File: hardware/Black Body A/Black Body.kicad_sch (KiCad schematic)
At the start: 38 parts, among them IC2 MCP96L00T-E_MX, J1 53307-2471, J2 Conn_01x02, J3 Conn_01x04, J5 Conn_02x04_Top_Bottom, J7 Conn_02x03_Top_Bottom

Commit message: new layout 2.0
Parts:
- removed R11, R12: 1.5k, Resistor_SMD:R_0805_2012Metric, symbol Device:R_US
- J3: footprint Connector_Molex:Molex_Nano-Fit_105313-xx04_1x04_P2.50mm_Horizontal -> Connector_PinHeader_2.54mm:PinHeader_1x04_P2.54mm_Vertical
- renumbered Ra1 to R11, Rb1 to R12

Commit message: Updated layout and 3D models
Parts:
- C2: P/N (none) -> MLASU168SB5105KTNA01
- C3: P/N (none) -> MLASH168SB7104KTNA01
- DB_1, DB_2, DB_3, Heartbeat1: P/N (none) -> LS Q976.01-N1Q2-1
- F2: P/N (none) -> 3557-2
- FB1, FB2: P/N (none) -> 742792910
- GND1, TP_TC_1, TP_TC_2, TP_TC_F_1, TP_TC_F_2, VCC1: P/N (none) -> 5015
- I2C_SCL1, I2C_SDA1, INT1: P/N (none) -> TSW-101-07-G-S
- IC2: footprint Blackbody Footprint:QFN65P500X500X100-21N-D -> BlackBody:QFN65P500X500X100-21N-D; P/N (none) -> MCP96L00T-E/MX
- J2: footprint Connector_Molex:Molex_Nano-Fit_105313-xx02_1x02_P2.50mm_Horizontal -> utsvt_connectors:105313-2102
- J7: footprint Connector_Molex:Molex_Nano-Fit_105314-xx06_2x03_P2.50mm_Horizontal -> utsvt_connectors:105314-1306
- R1: P/N (none) -> CRCW080510K0FKEA
- R10, R4, R7, R8: P/N (none) -> CRCW08051K50FKEA
- R11: P/N (none) -> CRCW060310K0FKEI
- R12: P/N (none) -> CRCW060343K0FKEI
- R2, R3: P/N (none) -> CRCW06031K00FKEI
- R5, R6: P/N (none) -> CRCW0603100RFKEA
- R9: P/N (none) -> CRCW06030000Z0EE

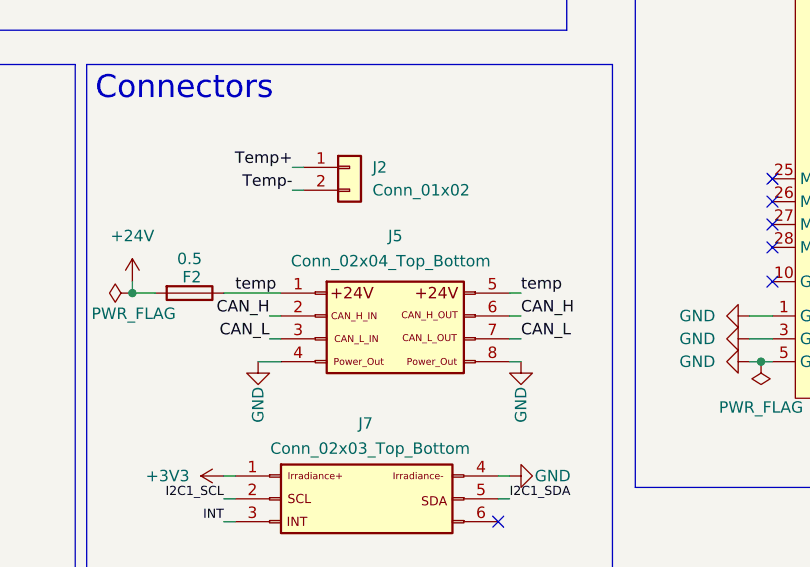
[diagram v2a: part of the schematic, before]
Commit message: changed 3D models for breakout
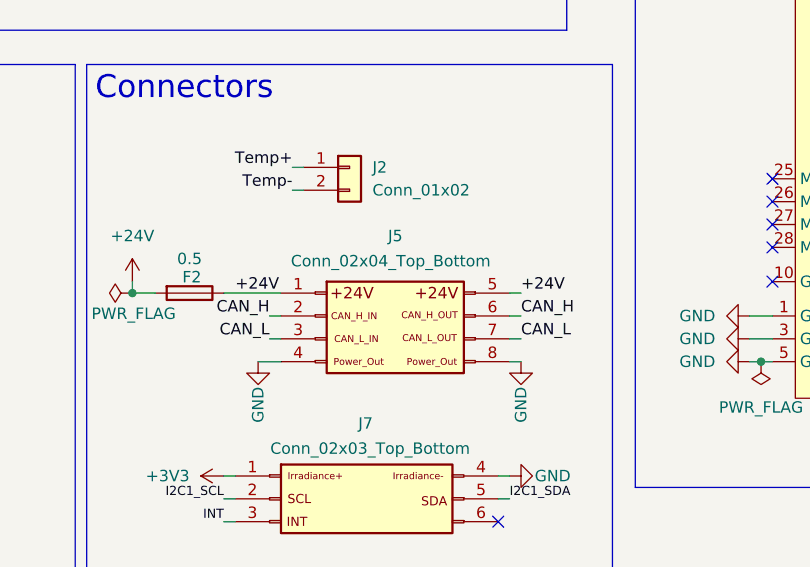
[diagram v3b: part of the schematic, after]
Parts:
- GND1, TP_TC_1, TP_TC_2, TP_TC_F_1, TP_TC_F_2, VCC1: footprint TestPoint:TestPoint_Pad_1.0x1.0mm -> TestPoint:TestPoint_Keystone_5005-5009_Compact
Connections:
- net temp is gone; now on net +24V: F2.1, J5.1 (Pin_1), J5.5 (Pin_5)
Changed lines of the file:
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@@
 		)
 	)
-	(label "temp"
+	(label "+24V"
 		(at 153.67 134.62 0)
 		(effects
@@
 		)
 	)
-	(label "temp"
+	(label "+24V"
 		(at 121.92 134.62 0)
 		(effects
@@
 			)
 		)
-		(property "Footprint" "TestPoint:TestPoint_Pad_1.0x1.0mm"
+		(property "Footprint" "TestPoint:TestPoint_Keystone_5005-5009_Compact"
 			(at 115.57 68.58 0)
 			(effects
@@
 			)
 		)
-		(property "Footprint" "TestPoint:TestPoint_Pad_1.0x1.0mm"
+		(property "Footprint" "TestPoint:TestPoint_Keystone_5005-5009_Compact"
 			(at 88.9 60.96 0)
 			(effects
@@
 			)
 		)
-		(property "Footprint" "TestPoint:TestPoint_Pad_1.0x1.0mm"
+		(property "Footprint" "TestPoint:TestPoint_Keystone_5005-5009_Compact"
 			(at 78.74 68.58 0)
 			(effects
@@
 			)
 		)
-		(property "Footprint" "TestPoint:TestPoint_Pad_1.0x1.0mm"
+		(property "Footprint" "TestPoint:TestPoint_Keystone_5005-5009_Compact"
 			(at 125.73 60.96 0)
 			(effects
@@
 			)
 		)
-		(property "Footprint" "TestPoint:TestPoint_Pad_1.0x1.0mm"
+		(property "Footprint" "TestPoint:TestPoint_Keystone_5005-5009_Compact"
 			(at 224.79 88.9 0)
 			(effects
@@
 			)
 		)
-		(property "Footprint" "TestPoint:TestPoint_Pad_1.0x1.0mm"
+		(property "Footprint" "TestPoint:TestPoint_Keystone_5005-5009_Compact"
 			(at 27.94 165.1 0)
 			(effects

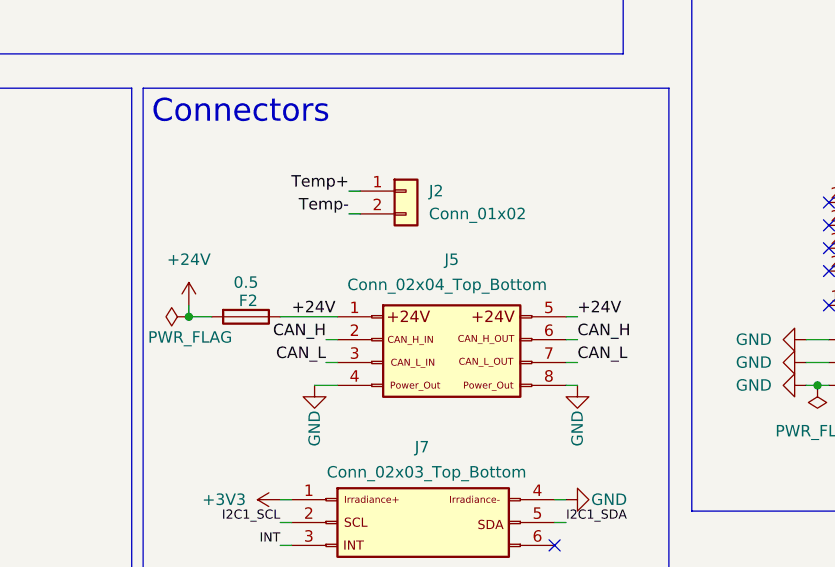
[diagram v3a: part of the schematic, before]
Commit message: updated 24V
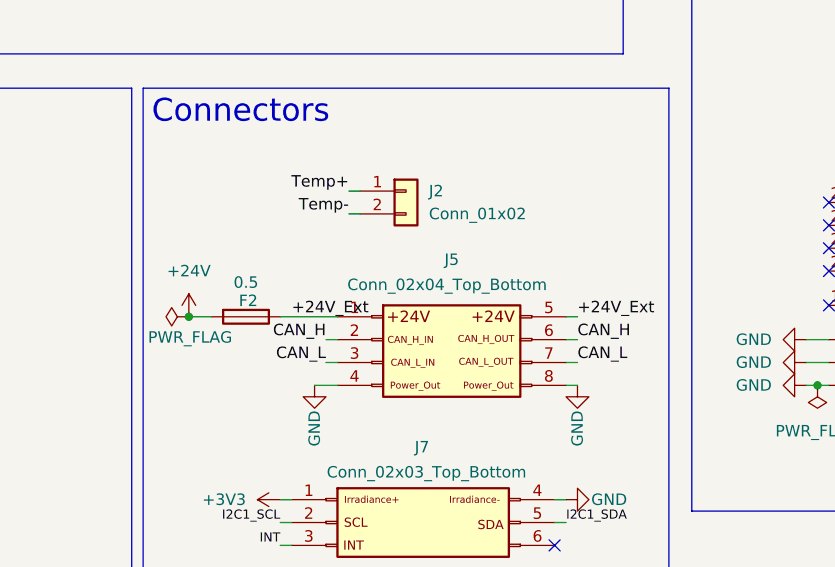
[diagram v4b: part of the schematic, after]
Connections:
- net +24V: no longer F2.1, J5.1 (Pin_1), J5.5 (Pin_5)
- new net +24V_Ext: F2.1, J5.1 (Pin_1), J5.5 (Pin_5)
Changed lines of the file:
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@@
 	)
 	(junction
-		(at 110.49 134.62)
-		(diameter 0)
-		(color 0 0 0 0)
-	)
-	(junction
 		(at 180.34 142.24)
 		(diameter 0)
@@
 	)
 	(junction
+		(at 110.49 134.62)
+		(diameter 0)
+		(color 0 0 0 0)
+	)
+	(junction
 		(at 120.65 60.96)
 		(diameter 0)
@@
 	(wire
 		(pts
-			(xy 110.49 133.35) (xy 110.49 134.62)
-		)
-		(stroke
-			(width 0)
-			(type default)
-		)
-	)
-	(wire
-		(pts
 			(xy 220.98 101.6) (xy 236.22 101.6)
 		)
@@
 		)
 	)
-	(label "+24V"
-		(at 153.67 134.62 0)
-		(effects
-			(font
-				(size 1.27 1.27)
-			)
-			(justify left bottom)
-		)
-	)
 	(label "INT"
 		(at 24.13 130.81 270)
@@
 		)
 	)
+	(label "+24V_Ext"
+		(at 153.67 134.62 0)
+		(effects
+			(font
+				(size 1.27 1.27)
+			)
+			(justify left bottom)
+		)
+	)
 	(label "DB_Conn_2"
 		(at 217.17 139.7 0)
@@
 		)
 	)
-	(label "+24V"
+	(label "+24V_Ext"
 		(at 121.92 134.62 0)
 		(effects
@@
 	)
 	(symbol
-		(lib_id "Connector:TestPoint")
-		(at 83.82 68.58 180)
+		(lib_id "power:+24V")
+		(at 110.49 134.62 0)
 		(unit 1)
 		(exclude_from_sim no)
@@
 		(dnp no)
 		(fields_autoplaced yes)
-		(property "Reference" "TP_TC_F_2"
-			(at 86.36 70.6119 0)
-			(effects
-				(font
-					(size 1.27 1.27)
-				)
-				(justify right)
-			)
-		)
-		(property "Value" "TestPoint"
-			(at 86.36 73.1519 0)
-			(effects
-				(font
-					(size 1.27 1.27)
-				)
-				(justify right)
-			)
-		)
-		(property "Footprint" "TestPoint:TestPoint_Keystone_5005-5009_Compact"
-			(at 78.74 68.58 0)
+		(property "Reference" "#PWR09"
+			(at 110.49 138.43 0)
 			(effects
 				(font
@@
 			)
 		)
-		(property "Datasheet" "~"
-			(at 78.74 68.58 0)
+		(property "Value" "+24V"
+			(at 110.49 129.54 0)
 			(effects
 				(font
 					(size 1.27 1.27)
 				)
-				(hide yes)
 			)
 		)
-		(property "Description" "test point"
-			(at 83.82 68.58 0)
+		(property "Footprint" ""
+			(at 110.49 134.62 0)
 			(effects
 				(font
@@
 			)
 		)
-		(property "Sim.Device" ""
-			(at 83.82 68.58 0)
+		(property "Datasheet" ""
+			(at 110.49 134.62 0)
 			(effects
 				(font
@@
 			)
 		)
-		(property "P/N" "5015 "
-			(at 83.82 68.58 0)
+		(property "Description" "Power symbol creates a global label with name \"+24V\""
+			(at 110.49 134.62 0)
 			(effects
 				(font
@@
 			(project "Black Body"
 				(path "/326551d7-59c6-4bc5-b0df-e38f608d8925"
-					(reference "TP_TC_F_2")
+					(reference "#PWR09")
 					(unit 1)
 				)
@@
 	)
 	(symbol
-		(lib_id "power:+24V")
-		(at 110.49 133.35 0)
+		(lib_id "Connector:TestPoint")
+		(at 83.82 68.58 180)
 		(unit 1)
 		(exclude_from_sim no)
@@
 		(dnp no)
 		(fields_autoplaced yes)
-		(property "Reference" "#PWR013"
-			(at 110.49 137.16 0)
+		(property "Reference" "TP_TC_F_2"
+			(at 86.36 70.6119 0)
+			(effects
+				(font
+					(size 1.27 1.27)
+				)
+				(justify right)
+			)
+		)
+		(property "Value" "TestPoint"
+			(at 86.36 73.1519 0)
+			(effects
+				(font
+					(size 1.27 1.27)
+				)
+				(justify right)
+			)
+		)
+		(property "Footprint" "TestPoint:TestPoint_Keystone_5005-5009_Compact"
+			(at 78.74 68.58 0)
 			(effects
 				(font
@@
 			)
 		)
-		(property "Value" "+24V"
-			(at 110.49 128.27 0)
+		(property "Datasheet" "~"
+			(at 78.74 68.58 0)
 			(effects
 				(font
 					(size 1.27 1.27)
 				)
+				(hide yes)
 			)
 		)
-		(property "Footprint" ""
-			(at 110.49 133.35 0)
+		(property "Description" "test point"
+			(at 83.82 68.58 0)
 			(effects
 				(font
@@
 			)
 		)
-		(property "Datasheet" ""
-			(at 110.49 133.35 0)
+		(property "Sim.Device" ""
+			(at 83.82 68.58 0)
 			(effects
 				(font
@@
 			)
 		)
-		(property "Description" "Power symbol creates a global label with name \"+24V\""
-			(at 110.49 133.35 0)
+		(property "P/N" "5015 "
+			(at 83.82 68.58 0)
 			(effects
 				(font
@@
 			(project "Black Body"
 				(path "/326551d7-59c6-4bc5-b0df-e38f608d8925"
-					(reference "#PWR013")
+					(reference "TP_TC_F_2")
 					(unit 1)
 				)

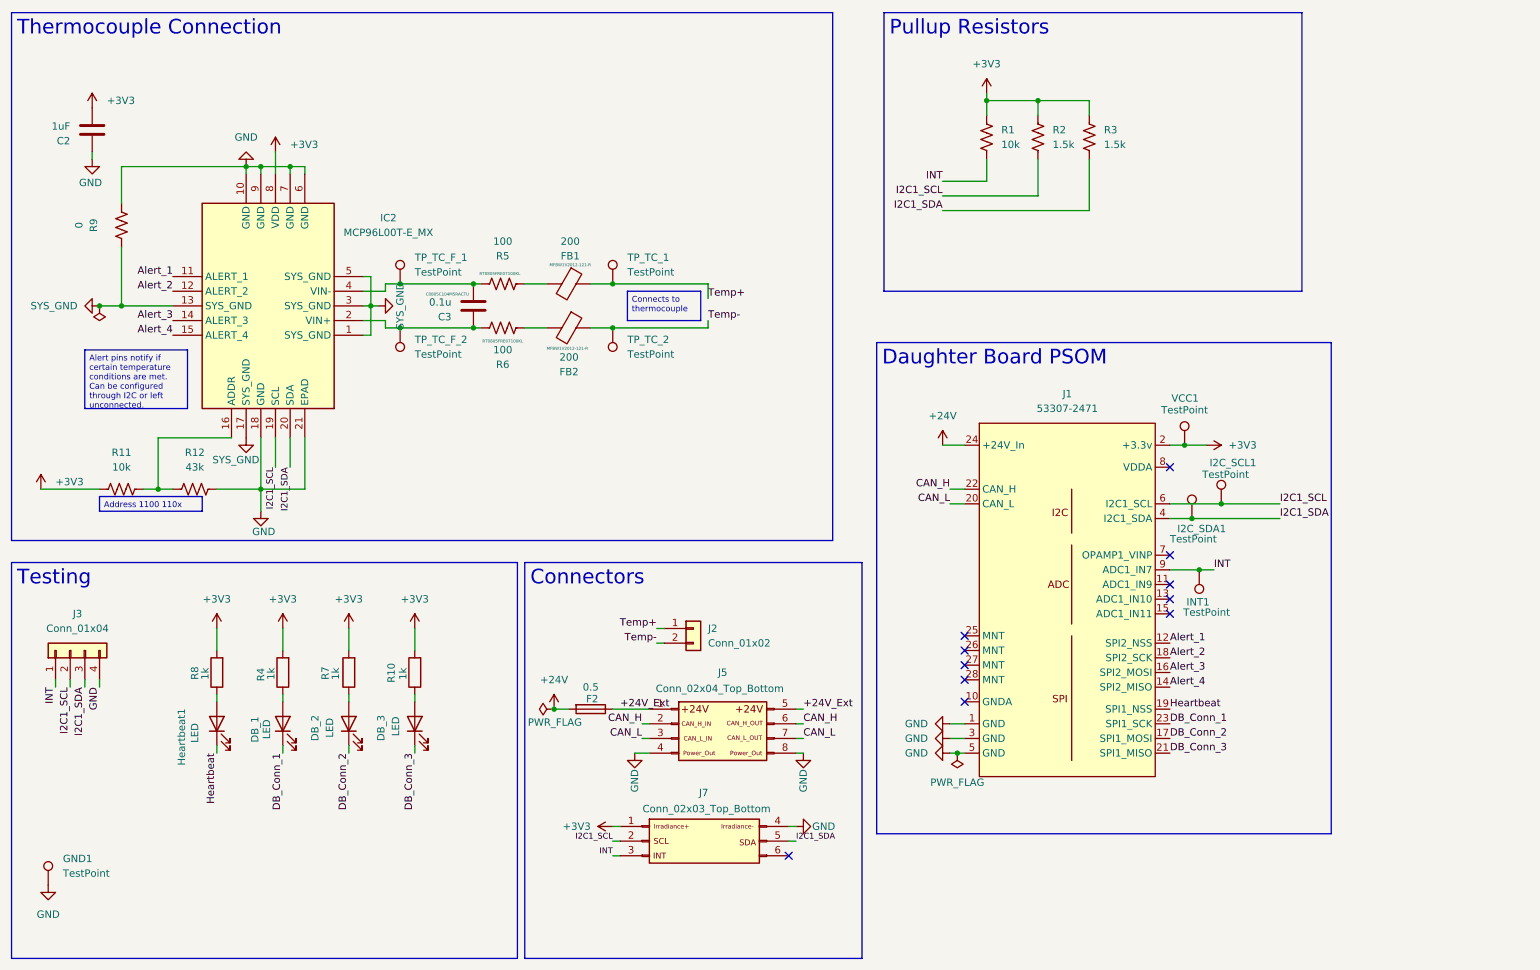
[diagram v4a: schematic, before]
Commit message: added logic analyzer + LEDS
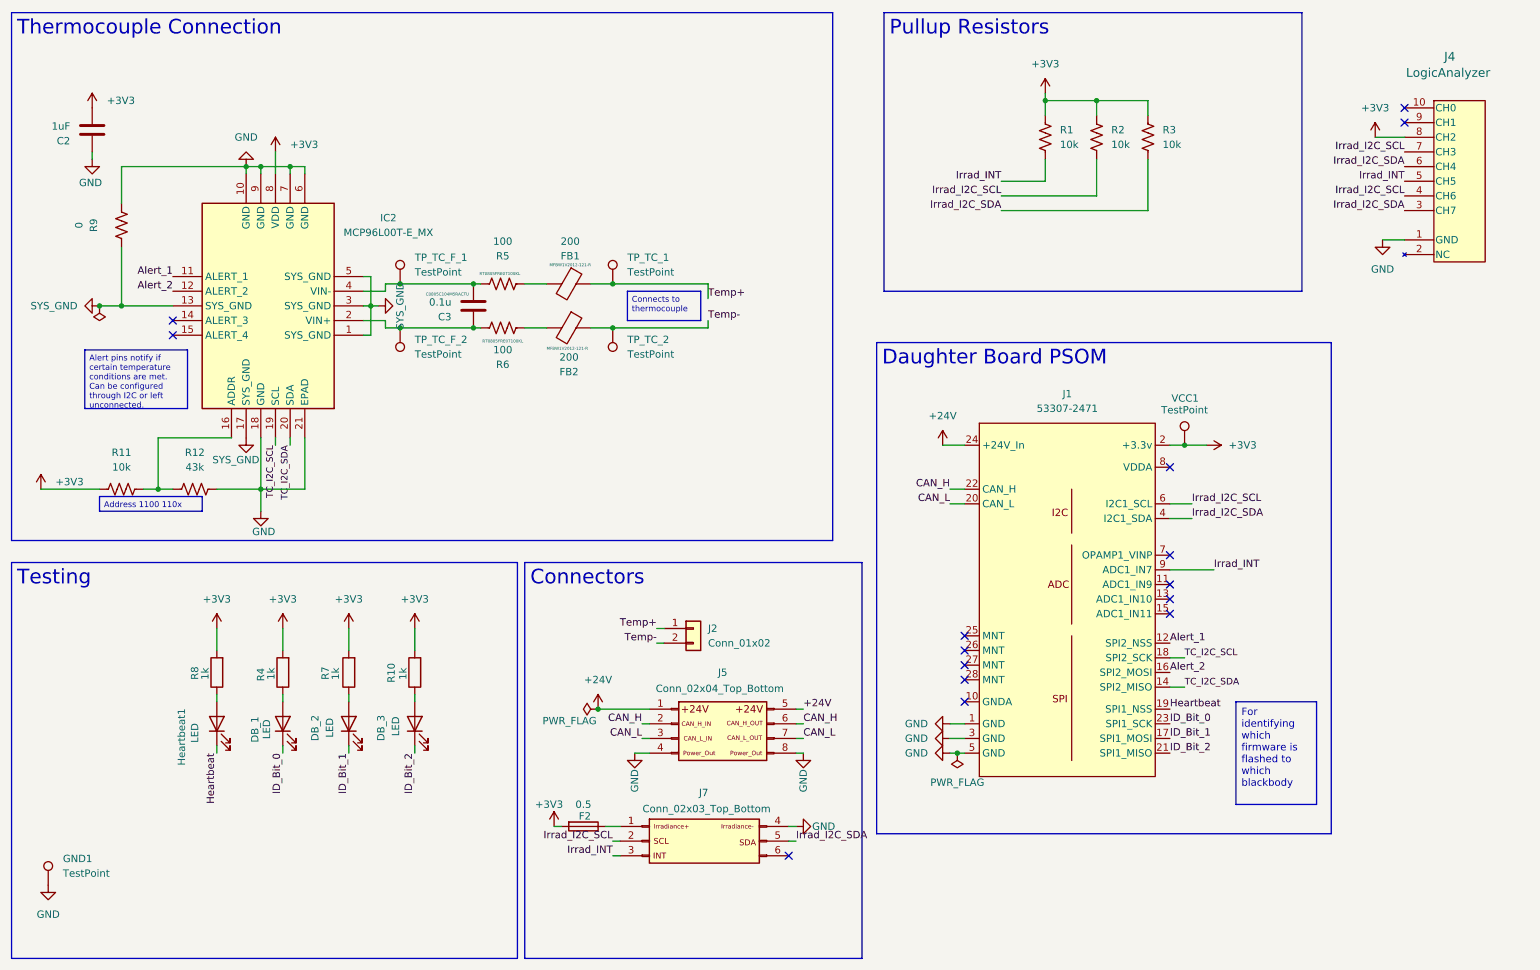
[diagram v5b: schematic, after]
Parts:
- removed I2C_SCL1, I2C_SDA1, INT1: TestPoint, Connector_PinHeader_2.54mm:PinHeader_1x01_P2.54mm_Vertical, symbol Connector:TestPoint
- removed J3: Conn_01x04, Connector_PinHeader_2.54mm:PinHeader_1x04_P2.54mm_Vertical, symbol Connector_Generic:Conn_01x04
- added J4: LogicAnalyzer, UTSVT_Connectors:CONN_SFH11-xxxC-D05-ST-XX_SUL, symbol utsvt_connectors:LogicAnalyzer
- R2, R3: value 1.5k -> 10k
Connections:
- net +24V: now also J5.1 (Pin_1), J5.5 (Pin_5); no longer F2.2
- net +3V3: now also F2.2, J4.8 (CH2); no longer J7.1 (Pin_1)
- net Alert_2: now also J1.16 (SPI2_MOSI); no longer J1.18 (SPI2_SCK)
- net GND: now also J4.1 (GND)
- removed net +24V_Ext: F2.1, J5.1 (Pin_1), J5.5 (Pin_5)
- net Alert_3: no longer names the net of IC2.14 (ALERT_3)
- net Alert_3: no longer J1.16 (SPI2_MOSI)
- net Alert_4: no longer names the net of IC2.15 (ALERT_4)
- net Alert_4: no longer J1.14 (SPI2_MISO)
- net DB_Conn_1 renamed ID_Bit_0
- net DB_Conn_2 renamed ID_Bit_1
- net DB_Conn_3 renamed ID_Bit_2
- net I2C1_SCL renamed Irrad_I2C_SCL
- net Irrad_I2C_SCL: now also J4.4 (CH6), J4.7 (CH3); no longer IC2.19 (SCL)
- net I2C1_SDA renamed Irrad_I2C_SDA
- net Irrad_I2C_SDA: now also J4.3 (CH7), J4.6 (CH4); no longer IC2.20 (SDA)
- net INT renamed Irrad_INT
- net Irrad_INT: now also J4.5 (CH5)
- new net: F2.1, J7.1 (Pin_1)
- new net TC_I2C_SCL: IC2.19 (SCL), J1.18 (SPI2_SCK)
- new net TC_I2C_SDA: IC2.20 (SDA), J1.14 (SPI2_MISO)
- no-connect marks 11 -> 15
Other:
- moved on the sheet: F2, R1, R2, R3
